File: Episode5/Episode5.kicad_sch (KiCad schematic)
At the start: 0 parts

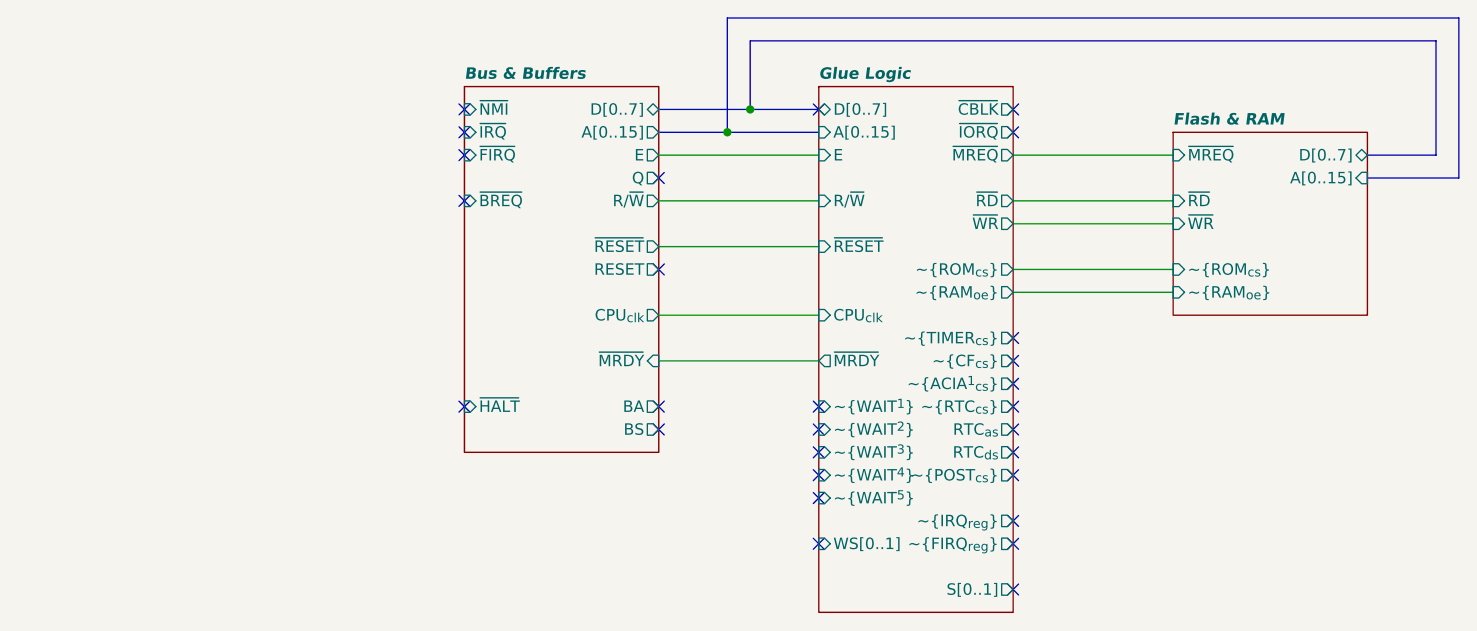
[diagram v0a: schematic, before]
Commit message: Placed Global labels instead. And toying with new PLDs
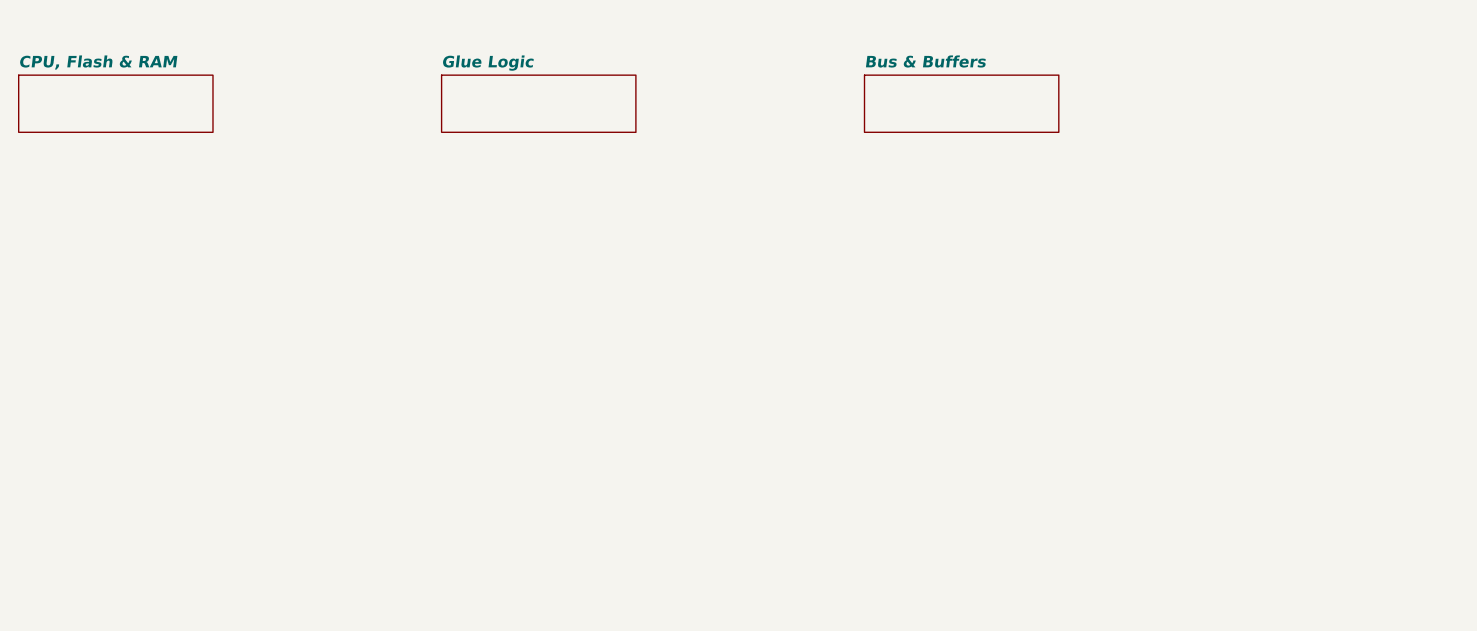
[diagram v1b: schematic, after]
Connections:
- no-connect marks 28 -> 0
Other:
- sheet Flash & RAM renamed CPU, Flash & RAM
- sheet Bus & Buffers ports: added none; removed A[0..15], BA, BS, CPU_{clk}, D[0..7], E, Q, RESET, R/~{W}, ~{BREQ}, ~{FIRQ}, ~{HALT}, ~{IRQ}, ~{MRDY}, ~{NMI}, ~{RESET}
- sheet CPU, Flash & RAM ports: added none; removed A[0..15], D[0..7], ~{MREQ}, ~{RAM_{oe}}, ~{RD}, ~{ROM_{cs}}, ~{WR}
- sheet Glue Logic ports: added none; removed A[0..15], CPU_{clk}, D[0..7], E, RTC_{as}, RTC_{ds}, R/~{W}, S[0..1], WS[0..1], ~{ACIA^{1}_{cs}}, ~{CBLK}, ~{CF_{cs}}, ~{FIRQ_{reg}}, ~{IORQ}, ~{IRQ_{reg}}, ~{MRDY}, ~{MREQ}, ~{POST_{cs}}, ~{RAM_{oe}}, ~{RD}, ~{RESET}, ~{ROM_{cs}}, ~{RTC_{cs}}, ~{TIMER_{cs}}, ~{WAIT^{1}}, ~{WAIT^{2}}, ~{WAIT^{3}}, ~{WAIT^{4}}, ~{WAIT^{5}}, ~{WR}

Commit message: Toying with different alternatives for the CPU board
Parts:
- added U13: 74LS07, symbol 74xx:74LS07
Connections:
- new net +5V: U13.14 (VCC)
- new net GND: U13.11, U13.13, U13.3, U13.5, U13.7 (GND), U13.9
- no-connect marks 0 -> 6
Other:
- sheet CPU, Flash & RAM renamed CPU, ROM & RAM
- sheet Bus & Buffers ports: added A[0..15], BA, BS, D[0..7], E, Q, R/~{W}, ~{BREQ}, ~{CBLK}, ~{FIRQ}[0..3], ~{HALT}, ~{IORQ}, ~{IRQ}[0..7], ~{MMU_{en}}, ~{MRDY}, ~{MREQ}, ~{RAM_{oe}}, ~{RD}, ~{RESET}, ~{WR}; removed none
- sheet CPU, ROM & RAM ports: added A[0..15], BA, BS, CPU_{clk}, D[0..7], E, Q, R/~{W}, ~{BREQ}, ~{FIRQ}, ~{HALT}, ~{IRQ}, ~{MMU_{en}}, ~{MRDY}, ~{MREQ}, ~{NMI}, ~{RAM_{oe}}, ~{RD}, ~{RESET}, ~{ROM_{cs}}, ~{WR}; removed none
- sheet Glue Logic ports: added A[0..15], CPU_{clk}, D[0..7], E, RTC_{as}, RTC_{ds}, R/~{W}, ~{ACIA^{1}_{cs}}, ~{CBLK}, ~{FIRQ}, ~{FIRQ}[0..3], ~{IORQ}, ~{IRQ}, ~{IRQ}[0..7], ~{MRDY}, ~{MREQ}, ~{RAM_{oe}}, ~{RD}, ~{RESET}, ~{ROM_{cs}}, ~{RTC_{cs}}, ~{TIMER_{cs}}, ~{WR}; removed none

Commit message: Finished the preliminary design of the CPU card
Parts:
- removed U13: 74LS07, symbol 74xx:74LS07
- added J1: SLOT, MicroHobbyist:72-pin CE connector, symbol MicroHobbyist:72-pin Card Edge (ISA style)
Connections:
- net +5V: now also J1.1 (A1), J1.2 (B1), J1.71 (A36), J1.72 (B36)
- net GND: now also J1.21 (A11), J1.22 (B11), J1.3 (A2), J1.4 (B2), J1.41 (A21), J1.42 (B21), J1.47 (A24), J1.48 (B24), J1.69 (A35), J1.70 (B35)
- new net +12V: J1.46 (B23)
- new net +3V3: J1.43 (A22), J1.44 (B22)
- new net -12V: J1.45 (A23)
- new net A0: J1.5 (A3)
- new net A1: J1.7 (A4)
- new net A10: J1.27 (A14)
- new net A11: J1.29 (A15)
- new net A12: J1.31 (A16)
- new net A13: J1.33 (A17)
- new net A14: J1.35 (A18)
- new net A15: J1.37 (A19)
- new net A2: J1.9 (A5)
- new net A3: J1.11 (A6)
- new net A4: J1.13 (A7)
- new net A5: J1.15 (A8)
- new net A6: J1.17 (A9)
- new net A7: J1.19 (A10)
- new net A8: J1.23 (A12)
- new net A9: J1.25 (A13)
- new net BA: J1.24 (B12)
- new net BS: J1.26 (B13)
- new net CLK_{cpu}: J1.28 (B14)
- new net D0: J1.53 (A27)
- new net D1: J1.55 (A28)
- new net D2: J1.57 (A29)
- new net D3: J1.59 (A30)
- new net D4: J1.61 (A31)
- new net D5: J1.63 (A32)
- new net D6: J1.65 (A33)
- new net D7: J1.67 (A34)
- new net E: J1.8 (B4)
- new net Q: J1.6 (B3)
- new net R/~{W}: J1.14 (B7)
- new net SPD_{cpu}: J1.30 (B15)
- new net ~{BREQ}: J1.36 (B18)
- new net ~{CART_{cs}}: J1.34 (B17)
- new net ~{CART_{det}}: J1.32 (B16)
- new net ~{CBLK}: J1.16 (B8)
- new net ~{FIRQ}1: J1.50 (B25)
- new net ~{FIRQ}2: J1.52 (B26)
- new net ~{FIRQ}3: J1.54 (B27)
- new net ~{HALT}: J1.38 (B19)
- new net ~{IORQ}: J1.18 (B9)
- new net ~{IRQ}1: J1.56 (B28)
- new net ~{IRQ}2: J1.58 (B29)
- new net ~{IRQ}3: J1.60 (B30)
- new net ~{IRQ}4: J1.62 (B31)
- new net ~{IRQ}5: J1.64 (B32)
- new net ~{IRQ}6: J1.66 (B33)
- new net ~{IRQ}7: J1.68 (B34)
- new net ~{MMU_{en}}: J1.51 (A26)
- new net ~{MRDY}: J1.40 (B20)
- new net ~{MREQ}: J1.20 (B10)
- new net ~{RAM_{oe}}: J1.49 (A25)
- new net ~{RD}: J1.10 (B5)
- new net ~{RESET}: J1.39 (A20)
- new net ~{WR}: J1.12 (B6)
- no-connect marks 6 -> 0
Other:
- sheet Bus & Buffers renamed CPU, Reset, Buffers
- sheet CPU, ROM & RAM renamed ROM, RAM, and RTC
- added sheet ACIA (Serial Ports) (ACIA.kicad_sch)
- added sheet Blinkenlights (Blinkenlights.kicad_sch)
- added sheet Interrupt Controllers (Interrupts.kicad_sch)
- added sheet Timer (TIMER.kicad_sch)
- sheet CPU, Reset, Buffers ports: added CLK_{cpu}, ~{FIRQ}, ~{IRQ}, ~{NMI}; removed ~{CBLK}, ~{FIRQ}[0..3], ~{IORQ}, ~{IRQ}[0..7], ~{MMU_{en}}, ~{MREQ}, ~{RAM_{oe}}, ~{RD}, ~{WR}
- sheet Glue Logic ports: added CLK_{cpu}, SPD_{cpu}, ~{CART_{cs}}, ~{CART_{det}}, ~{CONF_{cs}}, ~{FIRQ_{reg}}, ~{HALT}, ~{IRQ_{reg}}, ~{POST_{cs}}; removed CPU_{clk}, ~{FIRQ}, ~{FIRQ}[0..3], ~{IRQ}, ~{IRQ}[0..7]
- sheet ROM, RAM, and RTC ports: added RTC_{as}, RTC_{ds}, SQW, ~{IRQ}[0..7], ~{RTC_{cs}}; removed BA, BS, CPU_{clk}, E, Q, ~{BREQ}, ~{FIRQ}, ~{HALT}, ~{IRQ}, ~{MRDY}, ~{NMI}
- note added: "6309 Unleashed 2.0: Full-Featured Retro Computer Build"
- note added: "Schematic Hierarchical View"
- company: Frédéric "MicroHobbyist" Segard -> MicroHobbyist
